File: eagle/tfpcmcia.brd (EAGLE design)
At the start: 80.4 x 44.4 mm, 47 parts, among them IC1 CH32V307, IC2 LM1117MPX-3.3, IC3 APS6404L, IC4 MCP6001RT-I_OT, J2 MSD-11-A

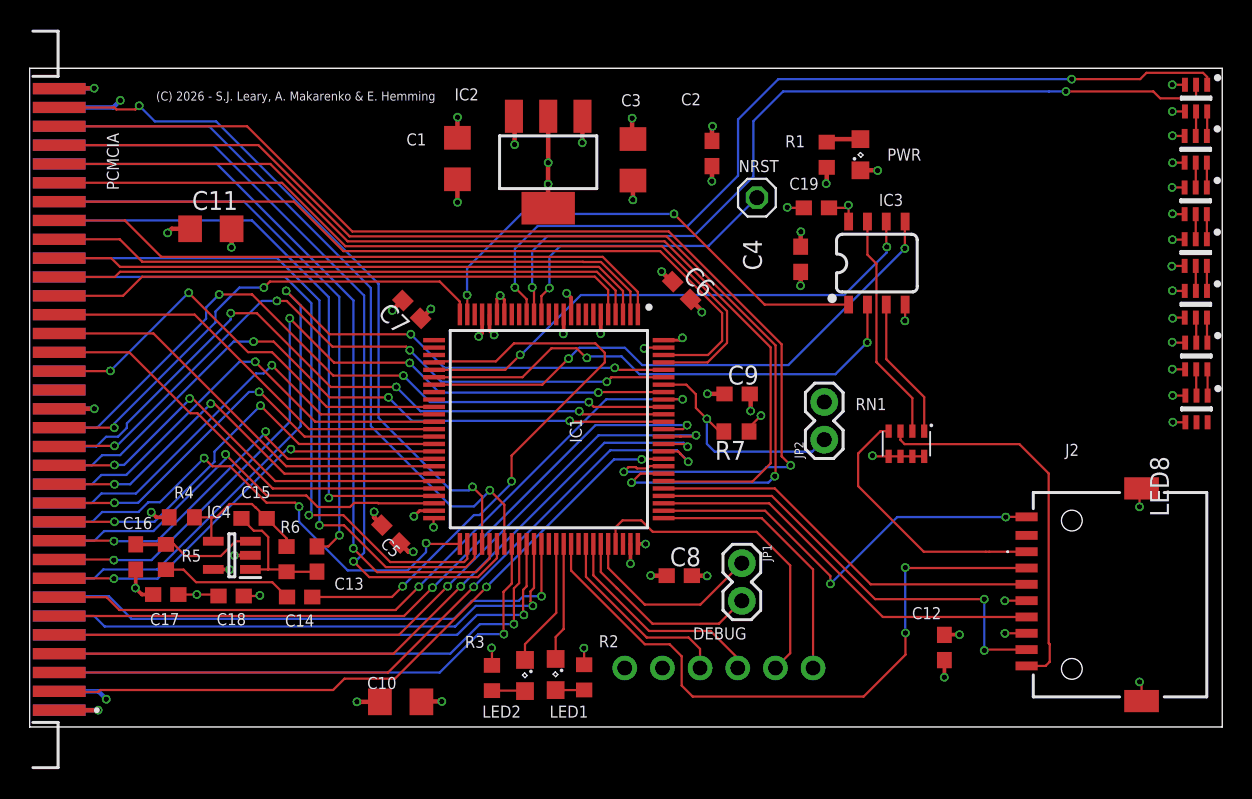
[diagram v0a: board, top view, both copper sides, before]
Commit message: CH32V467 upgrade
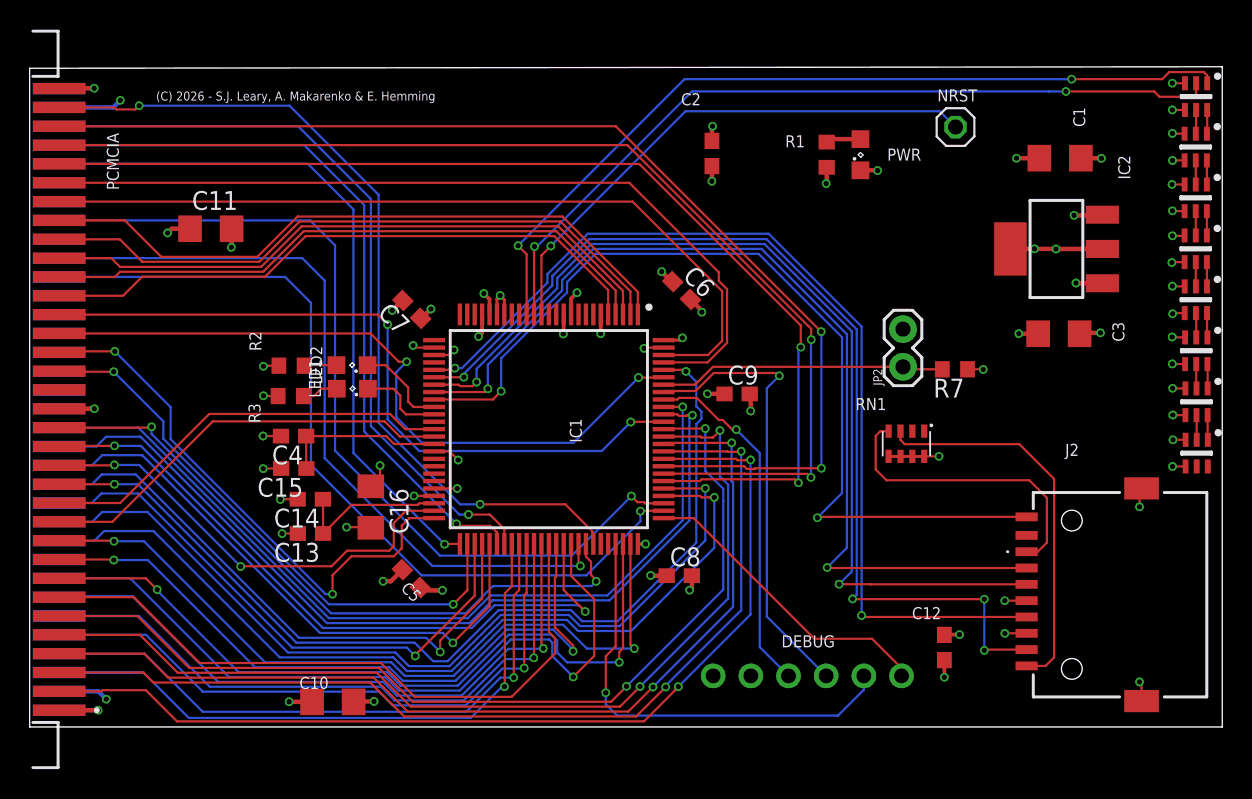
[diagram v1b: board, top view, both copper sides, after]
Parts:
- removed C17, C19: 1uF, eagle-ltspice:C0603
- removed C18: 100nF, eagle-ltspice:C0603
- removed IC3: APS6404L, SparkFun-IC-Memory:SO08
- removed IC4: MCP6001RT-I_OT, SamacSys_Parts:SOT95P270X145-5N
- removed JP1: (no value), SparkFun-Retired:1X02
- removed R4, R5, R6: 10k, rcl:R0603
- added LED10: COM-14608, Blinkenlights:SON75P200X200X100-6N
- C13: value 4.7uF -> 100nF
- C14: value 4.7uF -> 2.2uF
- C15: value 1nF -> 2.2uF
- C16: value 1nF -> 22uF; device eagle-ltspice:C0603 -> rcl:C1206
- IC1: value CH32V307 -> CH32V467
- moved C1 40.6 mm to (69.5, 38.3), turned to 180 degrees
- moved C4 36.2 mm to (17.8, 19.6), turned to 180 degrees
- moved IC2 34.8 mm to (69.2, 32.2), turned to 90 degrees
- moved C3 31.0 mm to (69.4, 26.5), turned to 0 degrees
- moved R2 28.8 mm to (17.7, 24.4), turned to 0 degrees
- moved LED1 25.0 mm to (21.7, 24.4), turned to 180 degrees
- moved R3 23.4 mm to (17.6, 22.3), turned to 0 degrees
- moved LED2 22.6 mm to (21.8, 22.8), turned to 180 degrees
- moved C16 16.2 mm to (23.0, 14.8)
- moved R7 15.3 mm to (62.4, 24.1)
- moved NRST 14.2 mm to (62.4, 40.4)
- moved JP2 7.23 mm to (58.9, 24.3)
- moved C14 6.63 mm to (18.9, 15.4)
- moved DEBUG 5.99 mm to (52.4, 3.44)
- moved C10 4.57 mm to (20.4, 1.70)
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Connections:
- removed net AUD_MIXED: C14.1, IC1.29
- removed net AUD_O: C13.1, PCMCIA.62
- removed net N$10: C15.1, IC4.4, R4.2, R6.1
- removed net N$7: C13.2, C15.2, IC4.1, R6.2
- removed net N$8: C16.1, IC4.3, R5.1
- removed net N$9: C14.2, R5.2
- removed net RAM_CLK: IC1.30, IC3.6
- removed net RAM_MISO: IC1.31, IC3.2
- removed net RAM_MOSI: IC1.32, IC3.5
- removed net RAM_SNSS: IC1.24, IC3.1
- removed net USB1_DM: IC1.70, JP1.2
- removed net USB1_DP: IC1.71, JP1.1
- new net VDD18: C13.1, C14.1, IC1.48
- new net VDDK: C15.1, C4.1, IC1.40
- net !REG: now also IC1.78; no longer IC1.47
- net !WAIT: now also IC1.67; no longer IC1.53
- net !WE: now also IC1.65; no longer IC1.95
- net A10: now also IC1.73; no longer IC1.41
- net A11: now also IC1.74; no longer IC1.42
- net A12: now also IC1.95; no longer IC1.43
- net A13: now also IC1.96; no longer IC1.44
- net A14: now also IC1.49; no longer IC1.45
- net A15: now also IC1.50; no longer IC1.46
- net A16: now also IC1.52; no longer IC1.35
- net A17: now also IC1.53; no longer IC1.36
- net A18: now also IC1.54; no longer IC1.37
- net A19: now also IC1.55; no longer IC1.89
- net A7: now also IC1.89; no longer IC1.38
- net A8: now also IC1.38; no longer IC1.39
- net A9: now also IC1.39; no longer IC1.40
- net CE1: now also IC1.63; no longer IC1.92
- net CE2: now also IC1.66; no longer IC1.96
- net D8: now also IC1.51; no longer IC1.55
- net GND: now also C13.2, C14.2, C15.2, IC1.27, IC1.41, IC1.47, LED10.3; no longer C17.2, C18.2, C19.2, IC1.49, IC1.74, IC3.4, IC4.5, R4.1
- net IORD: now also IC1.79; no longer IC1.48
- net IOWR: now also IC1.80; no longer IC1.51
- net LED1: now also IC1.35; no longer IC1.65
- net LED2: now also IC1.36; no longer IC1.64
- net N$3: now also LED10.2, LED9.5; no longer IC3.7, RN1.2
- net N$4: now also LED10.1, LED9.6; no longer IC3.3, RN1.1
- net OE: now also IC1.64; no longer IC1.93
- net READY: now also IC1.68; no longer IC1.25
- net RESET: now also IC1.77; no longer IC1.52
- net SD_CD: now also IC1.34; no longer IC1.77
- net SD_CLK: now also IC1.30; no longer IC1.78
- net SD_MISO: now also IC1.31; no longer IC1.79
- net SD_MOSI: now also IC1.32; no longer IC1.80
- net SD_SNSS: now also IC1.33; no longer IC1.66
- net USART_RX: now also IC1.93; no longer IC1.69
- net USART_TX: now also IC1.92; no longer IC1.68
- net VCC: now also LED10.4; no longer C17.1, C18.1, IC4.2
- net VCC33: now also C16.1, IC1.28, IC1.46; no longer C19.1, C4.1, IC1.50, IC3.8
- net WP/!IOCS16: now also IC1.69; no longer IC1.54
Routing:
- net AUD_MIXED: track 40.3 -> 0.00 mm, vias 2 -> 0
- net AUD_O: track 39.4 -> 0.00 mm, vias 1 -> 0
- net SD_CLK: track 27.6 -> 66.2 mm, vias 0 -> 2
- net SD_MOSI: track 27.2 -> 65.6 mm, vias 0 -> 2
- net RAM_MOSI: track 38.3 -> 0.00 mm, vias 2 -> 0
- net SD_MISO: track 30.8 -> 68.9 mm, vias 2 -> 4
- net A13: track 29.5 -> 65.5 mm
- net RAM_CLK: track 35.9 -> 0.00 mm, vias 2 -> 0
- net RAM_MISO: track 34.3 -> 0.00 mm, vias 2 -> 0
- net SD_CD: track 28.7 -> 62.6 mm
- net RAM_SNSS: track 32.9 -> 0.00 mm, vias 2 -> 0
- net IORD: track 29.5 -> 59.3 mm
- net IOWR: track 33.7 -> 58.6 mm, vias 3 -> 1
- net A10: track 29.0 -> 51.6 mm
- net A11: track 29.4 -> 51.8 mm
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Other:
- board size 80.4 x 44.4 mm -> 80.4 x 44.5 mm

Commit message: CH32V467 upgrade
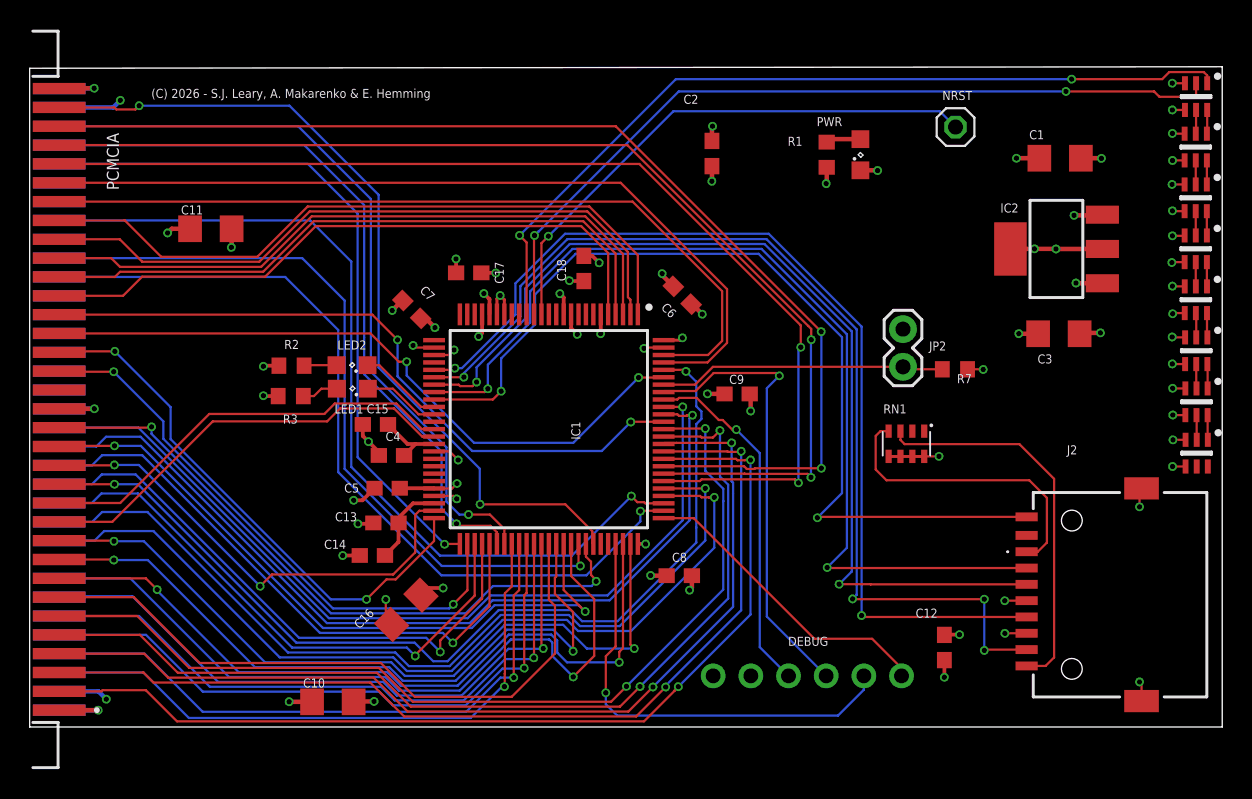
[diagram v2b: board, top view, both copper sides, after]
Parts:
- added C17, C18: 100nF, eagle-ltspice:C0603
- moved C16 7.33 mm to (25.4, 7.90), turned to 225 degrees
- moved C4 6.73 mm to (24.4, 18.3)
- moved C5 6.31 mm to (24.1, 16.1), turned to 180 degrees
- moved C15 6.25 mm to (23.3, 20.4)
- moved C14 5.65 mm to (23.1, 11.6)
- moved C13 5.14 mm to (24.0, 13.8)
- moved C6 0.32 mm to (44.0, 29.1), turned to 135 degrees
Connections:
- net GND: now also C17.2, C18.2
- net VCC33: now also C17.1, C18.1
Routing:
- net VDDK: track 11.0 -> 4.75 mm
- net VDD18: track 10.6 -> 5.72 mm
- net VCC33: track 37.1 -> 40.7 mm, vias 23 -> 24
- net GND: track 63.2 -> 65.9 mm, vias 40 -> 41
- net A12: track 48.8 -> 46.2 mm
- net A7: track 49.1 -> 46.8 mm
- net A6: track 41.8 -> 43.8 mm
- net A5: track 42.1 -> 44.1 mm
- net A2: track 44.8 -> 46.8 mm
- net A4: track 42.8 -> 44.8 mm
- net A3: track 43.8 -> 45.8 mm
- net A14: track 30.6 -> 32.3 mm
- net SD_CLK: track 66.2 -> 67.1 mm
- net SD_MISO: track 68.9 -> 69.7 mm
- net SD_MOSI: track 65.6 -> 66.4 mm
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
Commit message: final updates
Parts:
- C1: value 100nF -> 1uF
- C3: value 1uF -> 10uF
- moved C1 1.17 mm to (69.3, 37.2)
- moved C3 0.87 mm to (69.3, 27.4)
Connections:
- net GND: now also IC1.37
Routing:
- net GND: track 65.9 -> 68.6 mm, vias 41 -> 42
- net USART_RX: track 30.6 -> 30.0 mm
